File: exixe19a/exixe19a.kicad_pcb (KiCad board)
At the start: 2 copper layers, 20 x 40 mm, 39 parts, among them J1 Conn_01x07, J2 Conn_01x07, Q1 BF820W, Q10 BF820W, Q11 BF820W, Q3 MSB92W, Q4 BF820W, Q5 BF820W, Q6 BF820W, Q7 BF820W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

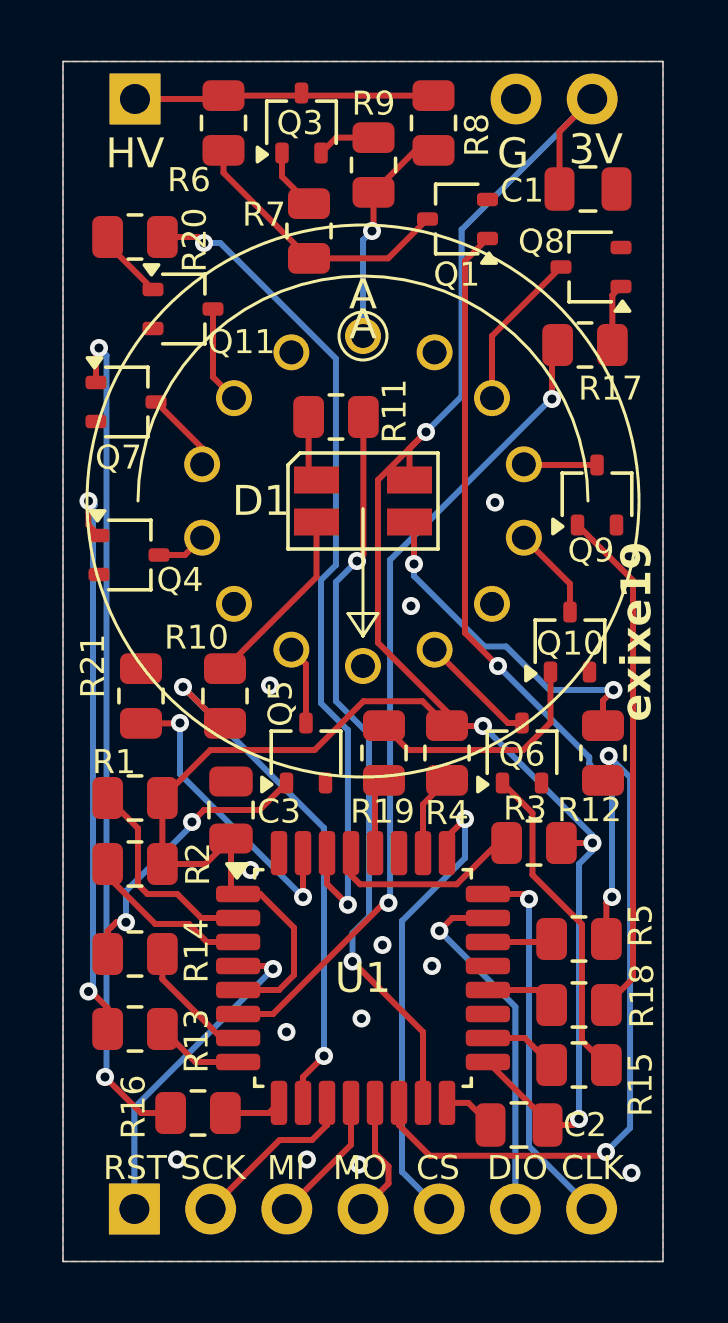
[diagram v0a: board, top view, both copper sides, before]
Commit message: Turns out I need to watch out for grounding planes that aren't actually connected to anything
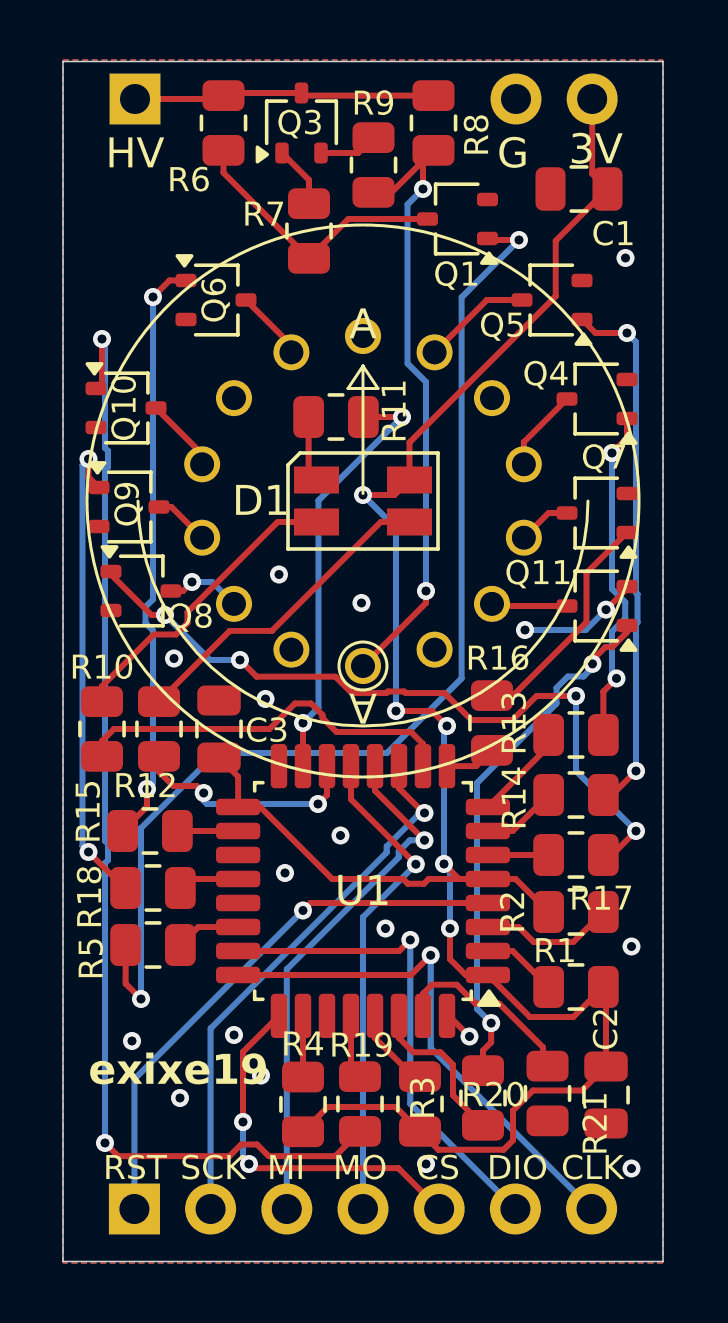
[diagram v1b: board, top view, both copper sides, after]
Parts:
- moved R20 31.0 mm to (44.0, 66.3), turned to 90 degrees
- moved R21 19.0 mm to (46.1, 66.2), turned to 90 degrees
- moved Q8 18.5 mm to (32.6, 49.4), turned to 0 degrees
- moved Q6 18.2 mm to (35.1, 39.7), turned to 0 degrees
- moved R13 17.7 mm to (47.1, 54.2), turned to 0 degrees
- moved Q5 17.2 mm to (46.3, 39.7), turned to 180 degrees
- moved R17 17.0 mm to (47.1, 58.2)
- moved Q11 17.0 mm to (47.8, 49.9), turned to 180 degrees
- moved Q10 16.7 mm to (32.1, 43.3), turned to 0 degrees
- moved Q4 16.4 mm to (47.8, 43.0), turned to 180 degrees
- moved R15 16.3 mm to (32.9, 57.4), turned to 180 degrees
- moved R16 16.3 mm to (44.3, 53.8), turned to 90 degrees
- moved Q7 16.1 mm to (47.8, 46.8), turned to 180 degrees
- moved R1 16.0 mm to (47.1, 62.6)
- moved R14 15.6 mm to (47.1, 56.2), turned to 0 degrees
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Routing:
- net Net-(Q10-B): track 7.95 -> 38.1 mm, vias 0 -> 2
- net /STM_5: track 27.5 -> 2.02 mm, vias 2 -> 0
- net /STM_4: track 28.3 -> 5.48 mm, vias 2 -> 0
- net Net-(Q8-B): track 2.07 -> 24.8 mm, vias 0 -> 4
- net Net-(Q7-B): track 28.3 -> 7.71 mm, vias 2 -> 0
- net Net-(Q11-B): track 2.38 -> 17.7 mm, vias 0 -> 2
- net /PWM_BLUE: track 22.8 -> 7.80 mm
- net +HV: track 7.51 -> 21.2 mm, vias 1 -> 2
- net /SPI_MISO: track 4.42 -> 17.6 mm, vias 0 -> 1
- net /SPI_MOSI: track 4.08 -> 16.6 mm, vias 0 -> 1
- net /SPI_SCK: track 5.78 -> 18.2 mm, vias 0 -> 1
- net Net-(Q1-B): track 25.8 -> 36.9 mm
- net /PWM_RED: track 24.9 -> 14.3 mm
- net Net-(Q6-B): track 10.8 -> 19.8 mm, vias 0 -> 2
- net Net-(Q5-B): track 9.44 -> 17.9 mm
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
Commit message: new version should work
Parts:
- moved R15 18.0 mm to (32.0, 39.4), turned to 90 degrees
- moved R13 17.5 mm to (33.1, 64.7), turned to 180 degrees
- moved R14 17.0 mm to (48.5, 39.3), turned to 90 degrees
- moved R17 15.4 mm to (31.8, 56.3), turned to 90 degrees
- moved R1 14.7 mm to (32.8, 59.4), turned to 0 degrees
- moved R2 14.4 mm to (32.8, 61.4)
- moved R21 14.1 mm to (37.6, 55.0), turned to -90 degrees
- moved R5 13.5 mm to (46.4, 59.7), turned to 90 degrees
- moved R4 12.2 mm to (41.9, 55.0), turned to -90 degrees
- moved R3 11.7 mm to (39.9, 55.0), turned to -90 degrees
- moved R20 11.2 mm to (44.7, 55.1), turned to 0 degrees
- moved R19 11.0 mm to (48.5, 59.7)
- moved R10 9.15 mm to (36.4, 46.4)
- moved R12 8.38 mm to (40.0, 49.1), turned to 180 degrees
- moved R18 7.10 mm to (31.8, 52.3), turned to 90 degrees
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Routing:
- net /STM_1: track 2.52 -> 39.9 mm, vias 0 -> 2
- net Net-(Q4-B): track 11.4 -> 43.8 mm, vias 2 -> 4
- net /STM_8: track 2.02 -> 32.4 mm, vias 0 -> 2
- net /STM_3: track 1.72 -> 28.0 mm, vias 0 -> 4
- net Net-(Q8-B): track 24.8 -> 3.01 mm, vias 4 -> 0
- net Net-(Q6-B): track 19.8 -> 2.89 mm, vias 2 -> 0
- net Net-(Q11-B): track 17.7 -> 2.16 mm, vias 2 -> 0
- net Net-(Q1-B): track 36.9 -> 22.2 mm
- net /STM_6: track 2.05 -> 16.6 mm, vias 0 -> 2
- net Net-(Q9-B): track 16.1 -> 1.71 mm, vias 2 -> 0
- net Net-(Q5-B): track 17.9 -> 3.79 mm, vias 2 -> 0
- net /SPI_MISO: track 17.6 -> 4.87 mm, vias 1 -> 0
- net /SPI_MOSI: track 16.6 -> 4.15 mm, vias 1 -> 0
- net /SPI_SCK: track 18.2 -> 5.96 mm, vias 1 -> 0
- net /PWM_BLUE: track 7.80 -> 19.7 mm
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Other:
- board text removed: "A"
